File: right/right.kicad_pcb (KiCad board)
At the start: 2 copper layers, 206.6 x 104.5 mm, 62 parts, among them J1 Modulo-Jack, J2 Modulo-Jack, J3 Modulo-Jack, SW1 SW_Push, SW10 SW_Push, SW11 SW_Push, SW12 SW_Push, SW13 SW_Push, SW14 SW_Push, SW15 SW_Push, SW16 SW_Push, SW17 SW_Push, SW18 SW_Push, SW19 SW_Push, SW2 SW_Push, SW20 SW_Push, SW21 SW_Push, SW22 SW_Push, SW23 SW_Push, SW24 SW_Push, SW25 SW_Push, SW26 SW_Push, SW27 SW_Push, SW28 SW_Push, SW29 SW_Push, SW3 SW_Push, SW30 SW_Push, SW31 SW_Push, SW32 SW_Push, SW33 SW_Push, SW34 SW_Push, SW35 SW_Push, SW36 SW_Push, SW37 SW_Push, SW38 SW_Push, SW39 SW_Push, SW4 SW_Push, SW40 SW_Push, SW41 SW_Push, SW42 SW_Push, SW43 SW_Push, SW5 SW_Push, SW6 SW_Push, SW7 SW_Push, SW8 SW_Push, SW9 SW_Push, U1 MCP23017_SP, U2 MCP23017_SP, U3 MCP23017_SP

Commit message: last commit
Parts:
- added ?: M2, lib:MountingHole_2.2mm_M2, F.Cu at (71.2, 121.1)
- added SW44: SW_DPDT_x2, lib:SlideSwitch_IS2235, F.Cu at (235.1, 115.6)
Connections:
- C1 pad 1: ADDR -> VCC
- D1 pad 2: ADDR -> VCC
- J1 pad D: ADDR -> VCC
- J2 pad D: ADDR -> VCC
- J3 pad D: ADDR -> VCC
- U1 pad 9: ADDR -> VCC
- U2 pad 15: ADDR -> VCC
- U2 pad 9: ADDR -> VCC
- U3 pad 16: ADDR -> VCC
- U3 pad 9: ADDR -> VCC
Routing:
- net ADDR: track 435.4 -> 65.4 mm, vias 3 -> 0
- net VCC: track 0.00 -> 366.7 mm, vias 0 -> 2
- net GND: track 1355.1 -> 1349.1 mm

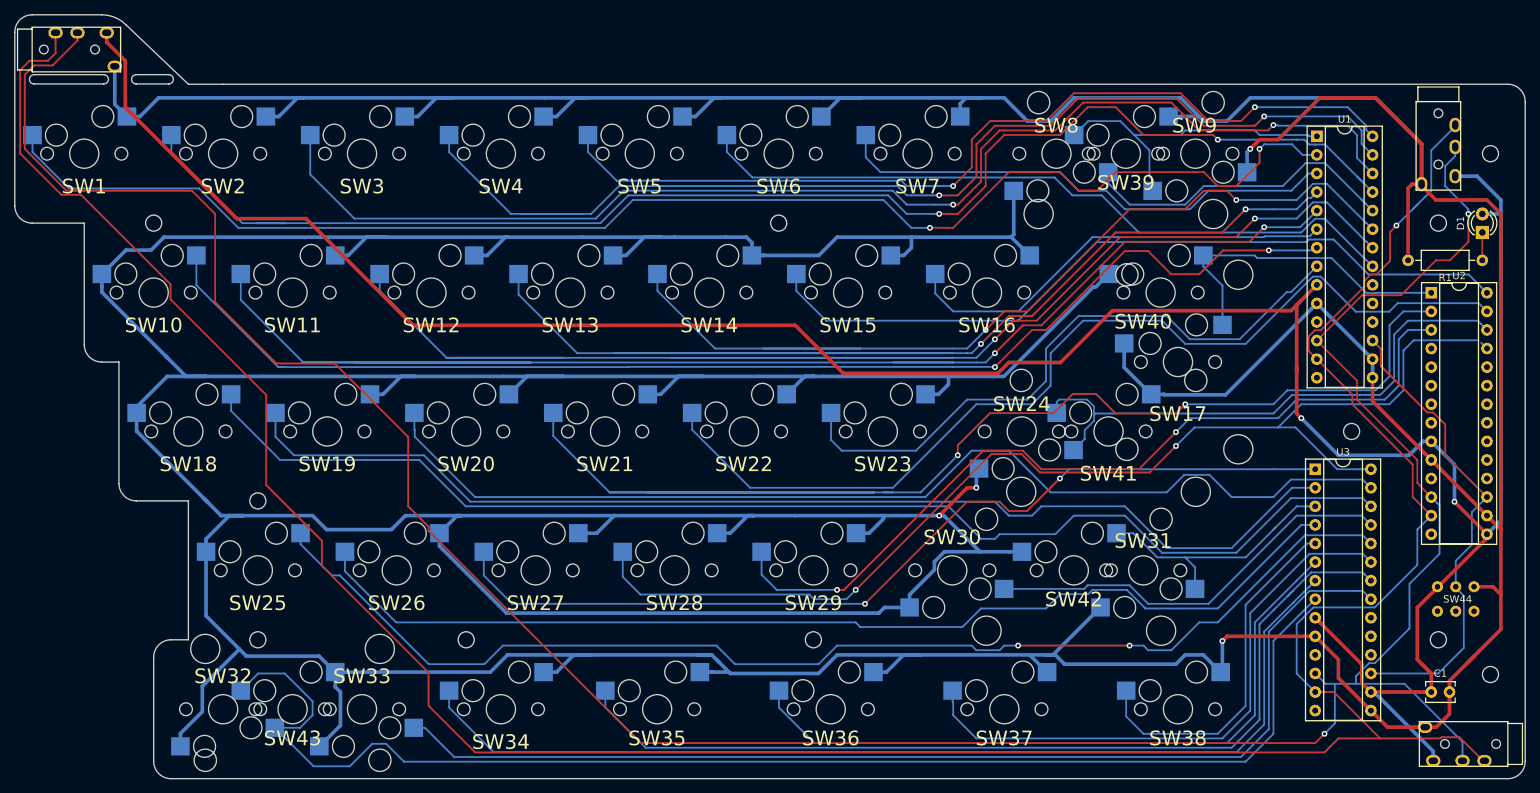
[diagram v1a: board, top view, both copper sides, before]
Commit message: modify right to JIS layout
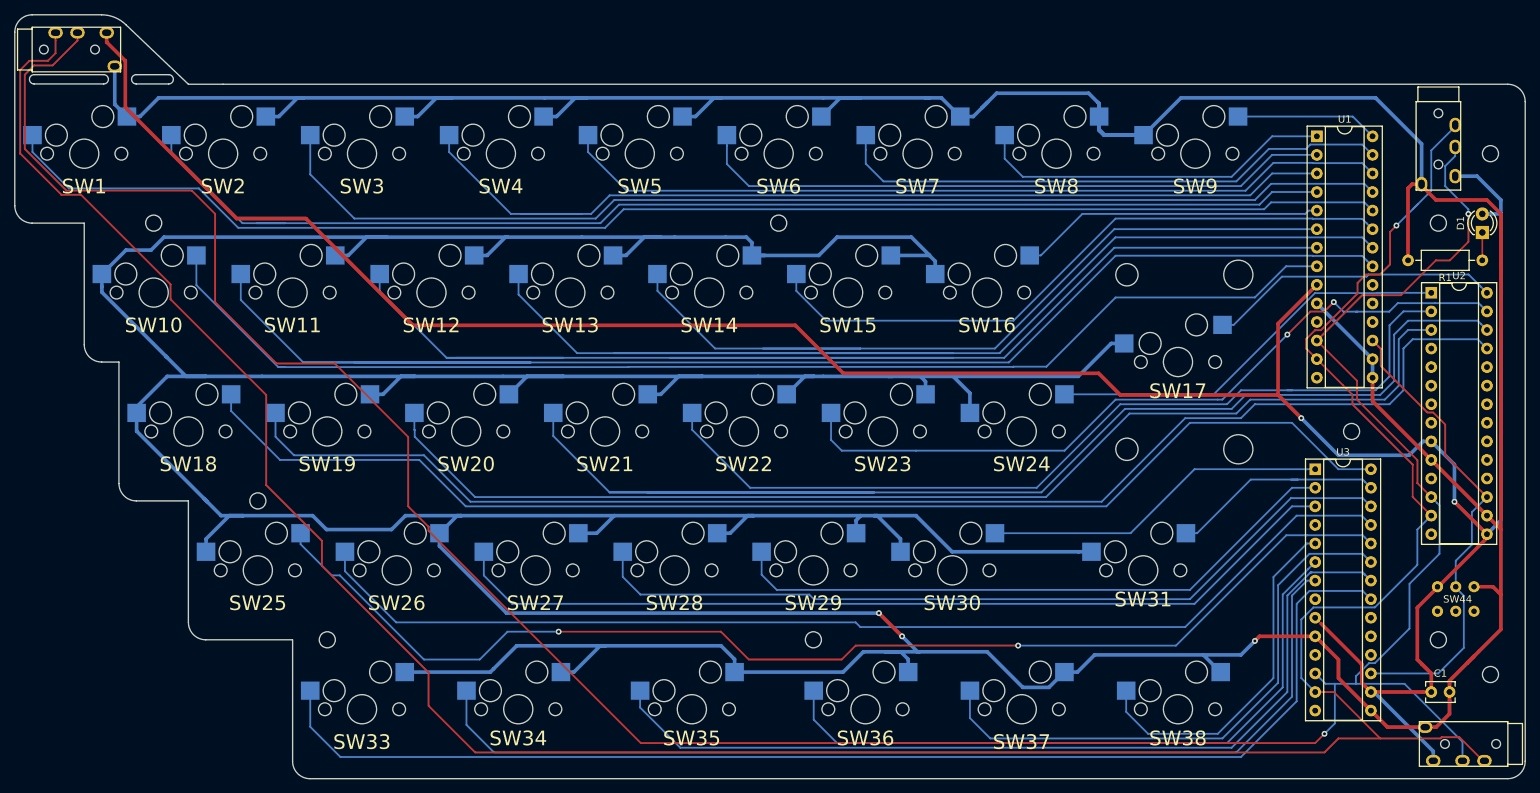
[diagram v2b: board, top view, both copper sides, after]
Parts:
- removed the ? at (71.2, 121.1)
- removed SW32: SW_Push, MX_Socket:MXOnly-1U-Hotswap
- removed SW39: SW_Push, MX_Socket:MXOnly-2U-Hotswap
- removed SW40: SW_Push, MX_Socket:MXOnly-1.5U-Hotswap
- removed SW41: SW_Push, MX_Socket:MXOnly-2.25U-Hotswap
- removed SW42: SW_Push, MX_Socket:MXOnly-2.75U-Hotswap
- removed SW43: SW_Push, MX_Socket:MXOnly-2U-Hotswap-ReversedStabilizers
- SW34: footprint MX_Socket:MXOnly-1U-Hotswap -> MX_Socket:MXOnly-1.25U-Hotswap
- SW37: footprint MX_Socket:MXOnly-1.25U-Hotswap -> MX_Socket:MXOnly-1U-Hotswap
- moved ? 19.0 mm to (80.8, 121.1)
- moved SW35 4.75 mm to (130.6, 130.6)
- moved SW36 4.75 mm to (154.4, 130.6)
- moved SW34 2.38 mm to (106.9, 130.6)
- moved SW37 2.38 mm to (175.8, 130.6)
- turned SW24 to 0 degrees
- turned SW30 to 0 degrees
- turned SW31 to 0 degrees
- turned SW33 to 0 degrees
- turned SW8 to 0 degrees
- turned SW9 to 0 degrees
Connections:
- SW16 pad 1: SW16 -> GND
- SW16 pad 2: GND -> SW16
- SW24 pad 1: SW24 -> GND
- SW24 pad 2: GND -> SW24
- SW30 pad 1: SW30 -> GND
- SW30 pad 2: GND -> SW30
- SW31 pad 1: SW31 -> GND
- SW31 pad 2: GND -> SW31
- U1 pad 1: SW9 -> SW8
- U1 pad 2: SW1 -> SW6
- U1 pad 21: SW6 -> SW11
- U1 pad 22: SW12 -> SW13
- U1 pad 23: SW14 -> SW15
- U1 pad 24: SW8 -> SW1
- U1 pad 25: SW2 -> SW3
- U1 pad 26: SW3 -> SW5
- U1 pad 27: SW4 -> SW7
- U1 pad 28: SW5 -> SW9
- U1 pad 3: SW7 -> SW4
- U1 pad 4: SW13 -> SW2
- U1 pad 5: SW11 -> SW16
- U1 pad 6: SW16 -> SW14
- U1 pad 7: SW10 -> SW12
- U1 pad 8: SW23 -> SW10
- U2 pad 1: SW17 -> SW24
- U2 pad 2: SW21 -> SW22
- U2 pad 25: Net-(U2-Pad25) -> SW19
- U2 pad 26: SW24 -> SW21
- U2 pad 27: SW22 -> SW23
- U2 pad 28: SW15 -> SW17
- U2 pad 3: SW29 -> SW20
- U3 pad 1: SW27 -> SW30
- U3 pad 2: SW19 -> SW29
- U3 pad 25: SW30 -> SW26
- U3 pad 26: SW18 -> SW28
- U3 pad 27: SW20 -> SW31
- U3 pad 28: SW28 -> SW18
- U3 pad 3: SW31 -> SW27
- U3 pad 4: SW26 -> Net-(U3-Pad4)
- U3 pad 8: SW32 -> Net-(U3-Pad8)
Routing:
- net SW32: track 183.6 -> 0.00 mm
- net GND: track 1349.1 -> 1171.8 mm, vias 4 -> 3
- net SW28: track 156.8 -> 113.2 mm, vias 2 -> 0
- net SW29: track 116.2 -> 85.5 mm, vias 2 -> 0
- net SW19: track 156.3 -> 185.8 mm
- net SW9: track 44.1 -> 19.5 mm
- net SW2: track 191.5 -> 168.6 mm, vias 2 -> 0
- net SW24: track 77.6 -> 56.4 mm
- net SW4: track 156.0 -> 135.1 mm, vias 2 -> 0
- net SW33: track 150.3 -> 169.4 mm
- net SW16: track 60.5 -> 41.8 mm
- net SW23: track 86.4 -> 104.1 mm, vias 0 -> 2
- net SW15: track 106.8 -> 89.2 mm
- net SW3: track 170.4 -> 155.6 mm, vias 2 -> 0
- net SW14: track 129.7 -> 115.9 mm, vias 2 -> 0
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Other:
- outline, holes or cut-outs redrawn
